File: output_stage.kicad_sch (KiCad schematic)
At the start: 24 parts

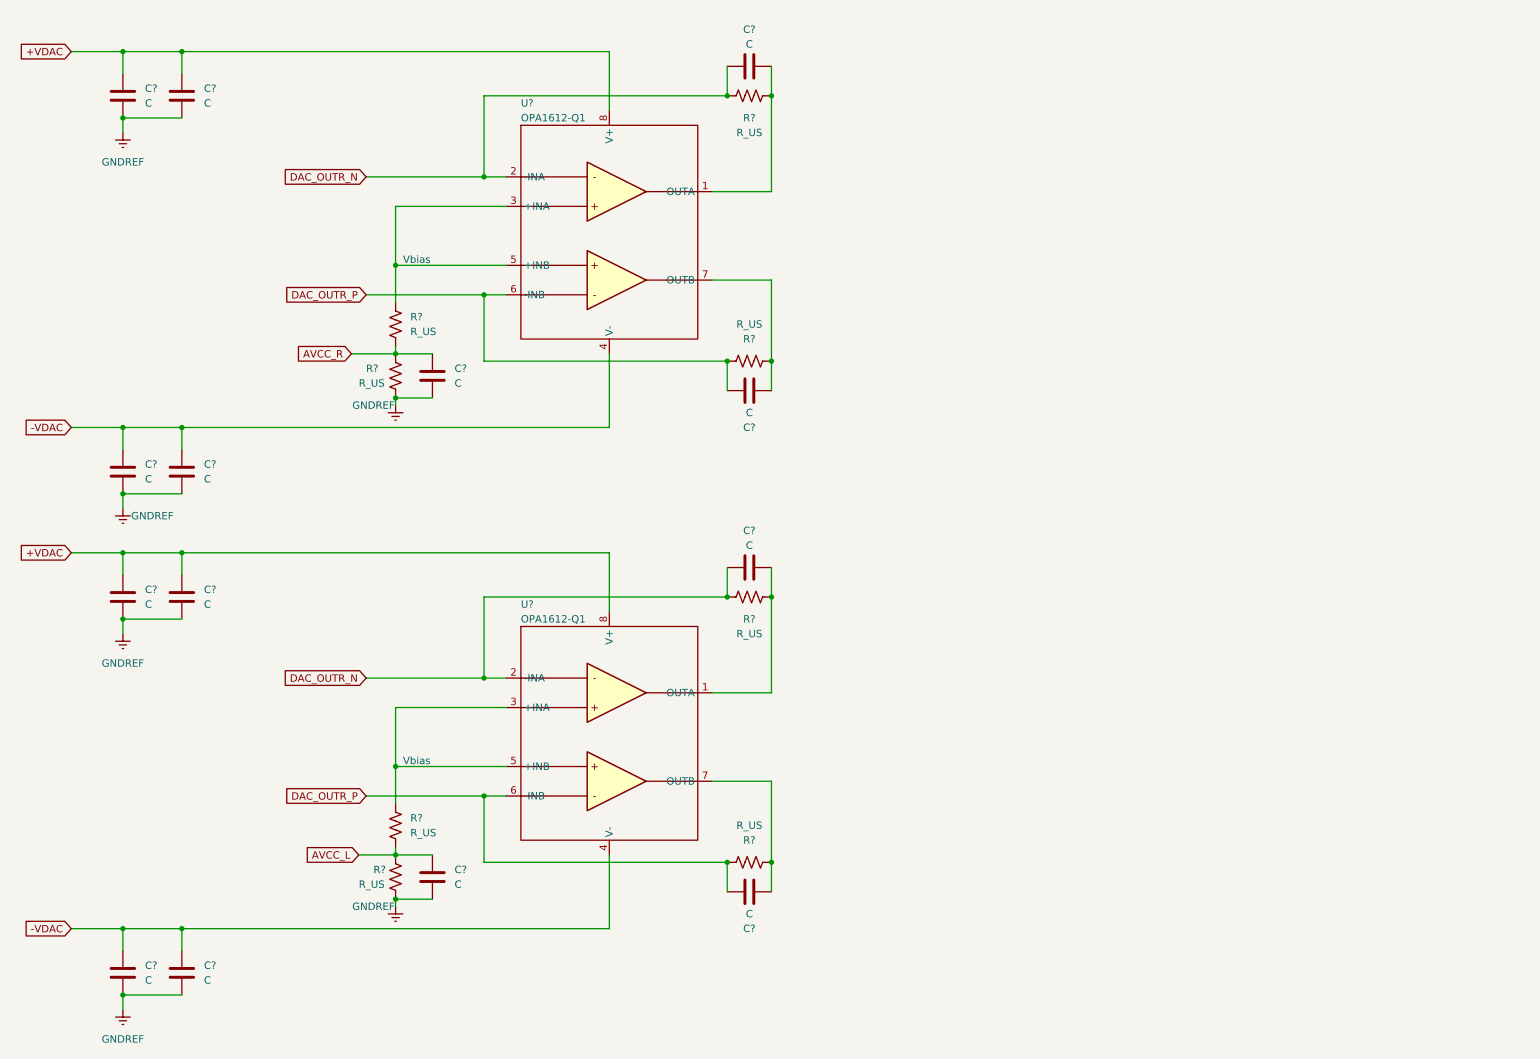
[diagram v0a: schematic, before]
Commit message: Adding values to output stage
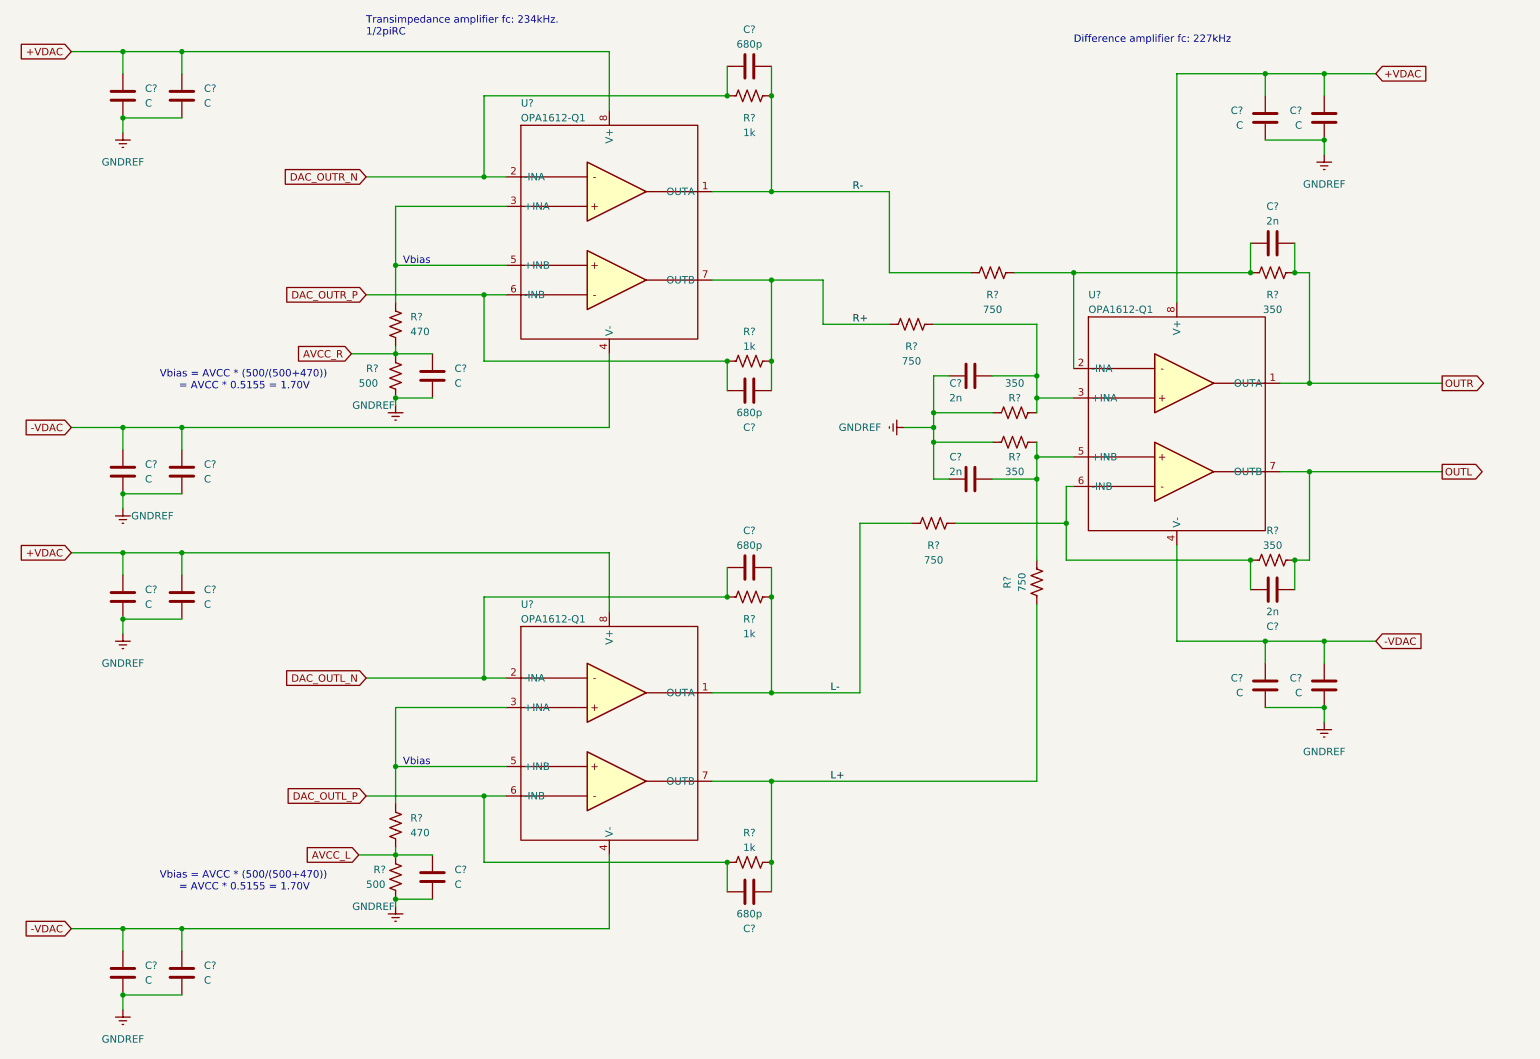
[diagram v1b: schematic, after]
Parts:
- added C? (x4): C, symbol Device:C
- added C? (x4): 2n, symbol Device:C
- added R? (x4): 750, symbol Device:R_US
- added R? (x4): 350, symbol Device:R_US
- added U?: OPA1612-Q1, symbol steDAC:OPA1612-Q1
- C? (x4): value C -> 680p
- R? (x2): value R_US -> 470
- R? (x2): value R_US -> 500
- R? (x4): value R_US -> 1k
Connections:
- net +VDAC: now also C?.2, C?.2, U?.8 (V+)
- net -VDAC: now also C?.2, C?.2, U?.4 (V-)
- net DAC_OUTR_N: no longer C?.2, R?.2, U?.2 (-INA)
- net DAC_OUTR_P: no longer C?.1, R?.1, U?.6 (-INB)
- net GNDREF: now also C?.1, C?.1, C?.1, C?.1, C?.1, C?.2, R?.1, R?.2
- net R+: now reaches C?.2, R?.2, U?.7 (OUTB)
- net R+: now also R?.2
- net R-: now reaches C?.1, R?.1, U?.1 (OUTA)
- net R-: now also R?.2
- net L-: now reaches C?.1, R?.1, U?.1 (OUTA)
- net L-: now also R?.2
- net L+: now reaches C?.2, R?.2, U?.7 (OUTB)
- net L+: now also R?.1
- new net: C?.2, R?.1, R?.2, U?.2 (-INA)
- new net: C?.1, R?.1, R?.1, U?.6 (-INB)
- new net: C?.1, R?.1, R?.2, U?.3 (+INA)
- new net: C?.2, R?.1, R?.2, U?.5 (+INB)
- new net DAC_OUTL_N: C?.2, R?.2, U?.2 (-INA)
- new net DAC_OUTL_P: C?.1, R?.1, U?.6 (-INB)
- new net OUTL: C?.2, R?.2, U?.7 (OUTB)
- new net OUTR: C?.1, R?.1, U?.1 (OUTA)
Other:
- note added: "Difference amplifier fc: 227kHz"
- note added: "Transimpedance amplifier fc: 234kHz. 1/2piRC"
- note added: "Vbias = AVCC * (500/(500+470)) = AVCC * 0.5155 = 1.70V"
- title: SteDAC Output Stage -> Output Stage

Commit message: Redoing power stage and changing output stage accordingly
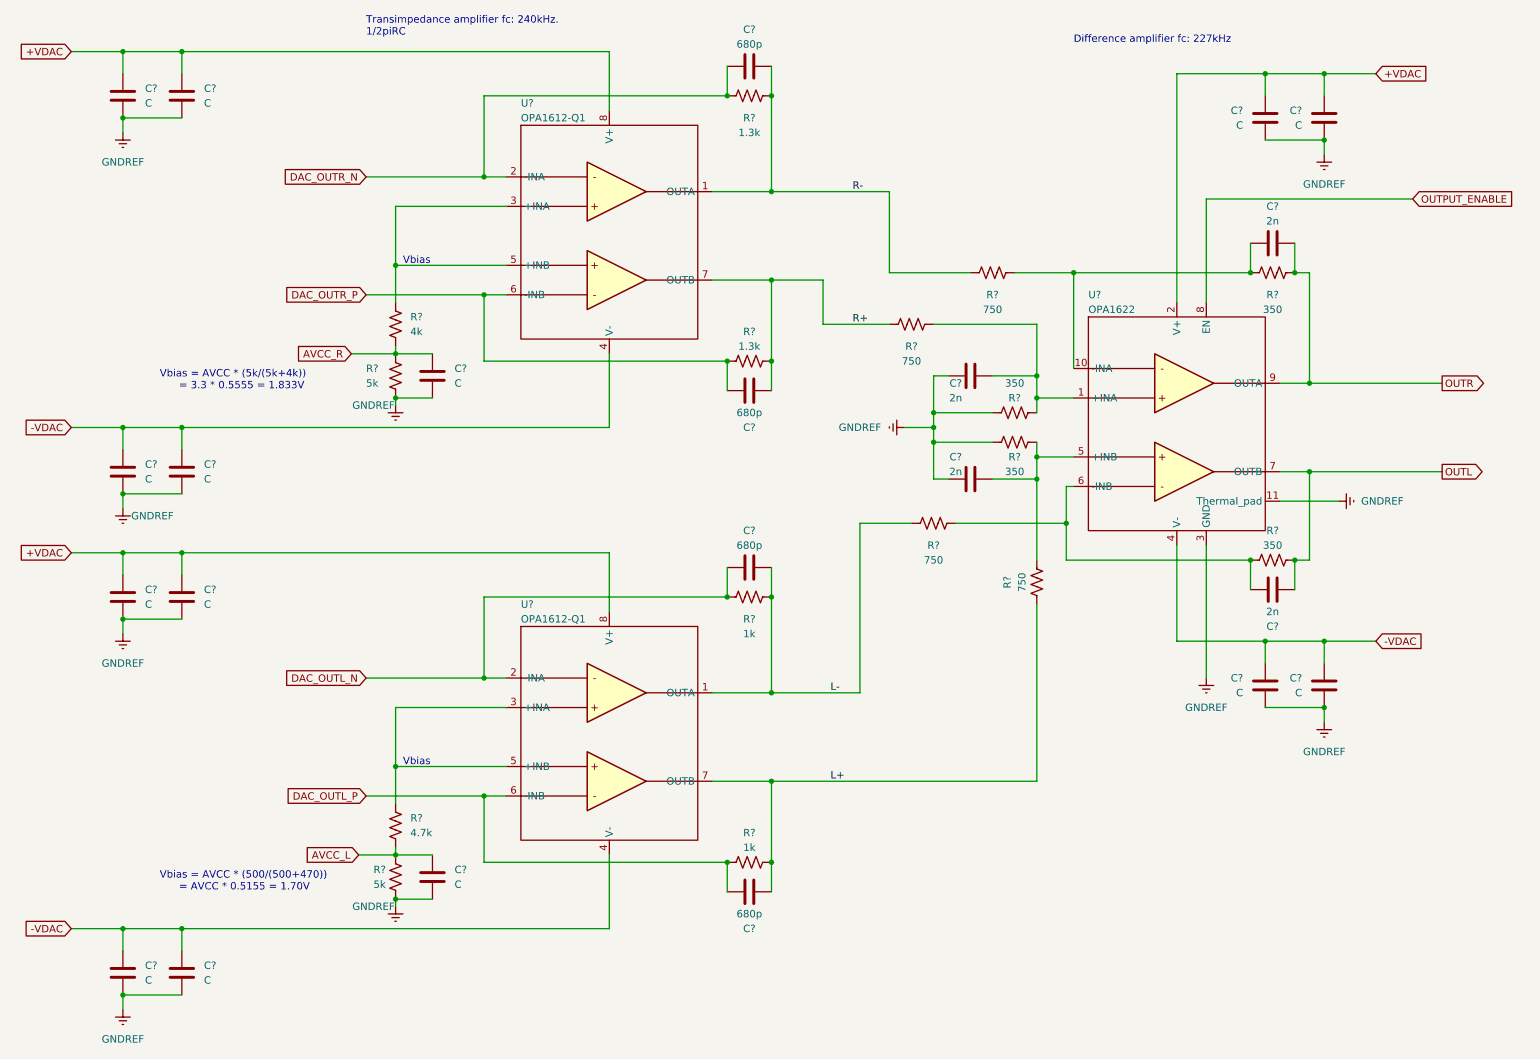
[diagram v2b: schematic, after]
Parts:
- removed U?: OPA1612-Q1, symbol steDAC:OPA1612-Q1
- added U?: OPA1622, symbol steDAC:OPA1622
- R?: value 470 -> 4.7k
- R? (x2): value 500 -> 5k
- R? (x2): value 1k -> 1.3k
- R?: value 470 -> 4k
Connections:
- net +VDAC: now also U?.2 (V+)
- net -VDAC: now also U?.4 (V-)
- net GNDREF: now also U?.11 (Thermal_pad), U?.3 (GND)
- net OUTL: now also U?.7 (OUTB)
- net OUTR: now also U?.9 (OUTA)
- net at C?.2, R?.1, R?.2: now also U?.10 (-INA)
- net at C?.1, R?.1, R?.1: now also U?.6 (-INB)
- net at C?.1, R?.1, R?.2: now also U?.1 (+INA)
- net at C?.2, R?.1, R?.2: now also U?.5 (+INB)
- new net OUTPUT_ENABLE: U?.8 (EN)
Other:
- note added: "Transimpedance amplifier fc: 240kHz. 1/2piRC"
- note added: "Vbias = AVCC * (5k/(5k+4k)) = 3.3 * 0.5555 = 1.833V"
- note removed: "Transimpedance amplifier fc: 234kHz. 1/2piRC"

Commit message: Finishing MCU interface. Adding connectors
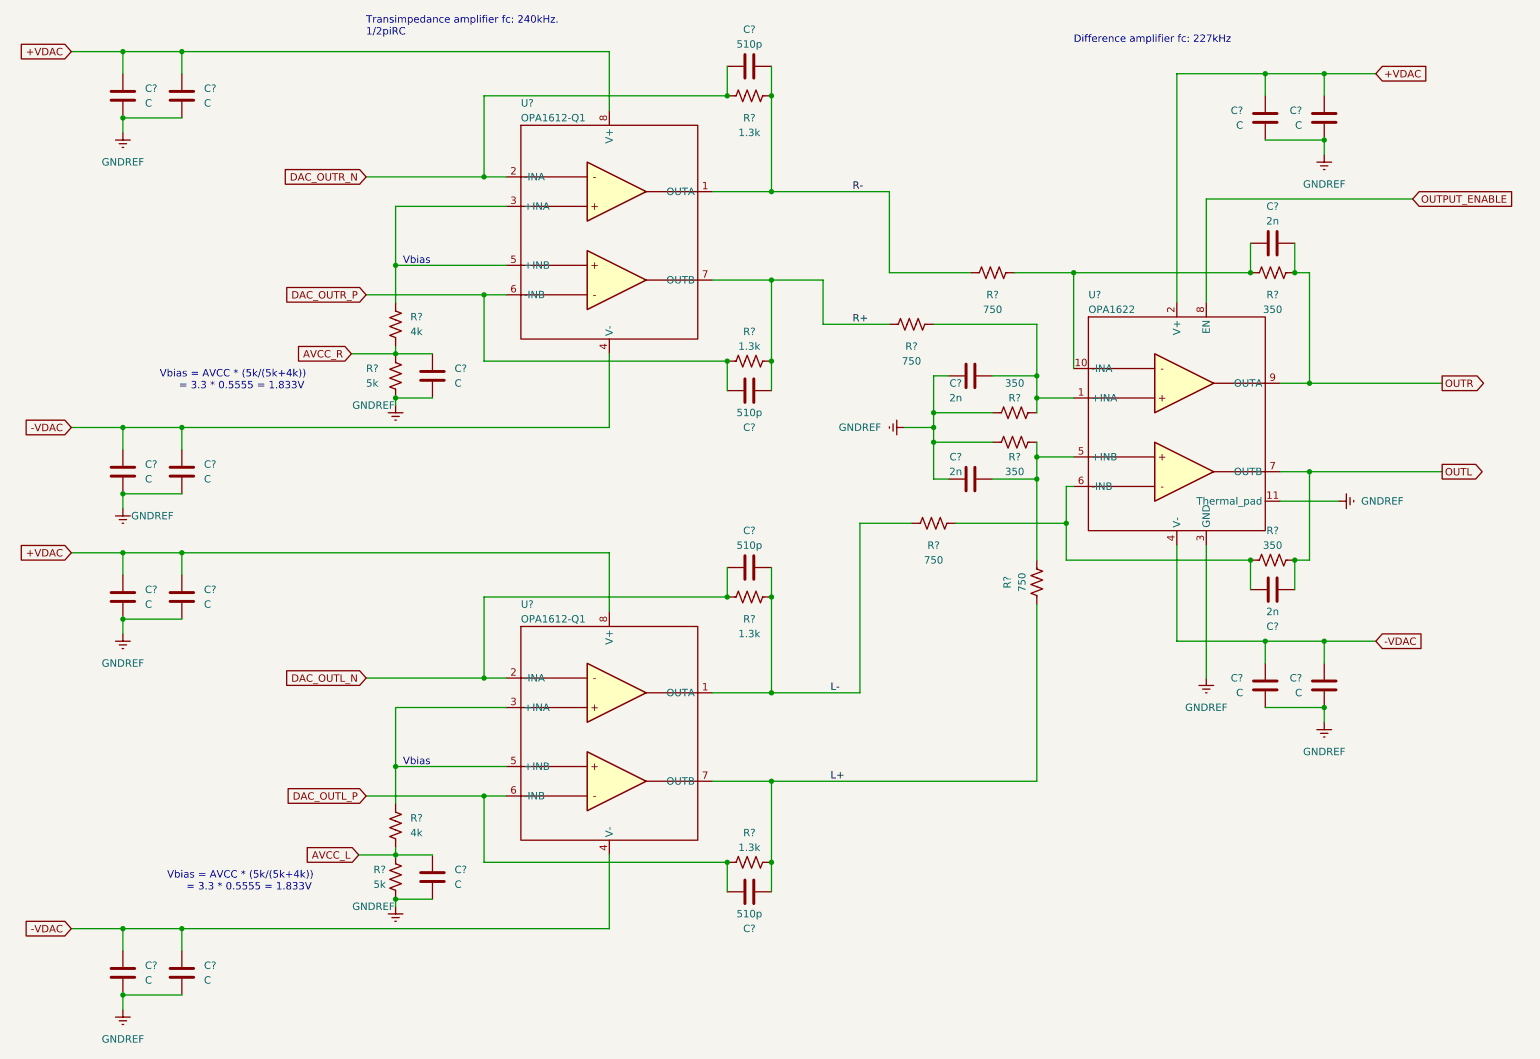
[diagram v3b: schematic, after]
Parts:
- C? (x4): value 680p -> 510p
- R?: value 4.7k -> 4k
- R? (x2): value 1k -> 1.3k
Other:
- note removed: "Vbias = AVCC * (500/(500+470)) = AVCC * 0.5155 = 1.70V"
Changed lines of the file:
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@@
     (stroke (width 0) (type default) (color 0 0 0 0))
   )
-  (text "Vbias = AVCC * (500/(500+470)) \n	  = AVCC * 0.5155 = 1.70V"
-    (at 41.91 163.83 0)
-    (effects (font (size 1.27 1.27)) (justify left bottom))
-  )
   (text "Transimpedance amplifier fc: 240kHz.\n1/2piRC" (at 77.47 16.51 0)
     (effects (font (size 1.27 1.27)) (justify left bottom))
@@
   )
   (text "Vbias" (at 83.82 55.88 0)
+    (effects (font (size 1.27 1.27)) (justify left bottom))
+  )
+  (text "Vbias = AVCC * (5k/(5k+4k)) \n	  = 3.3 * 0.5555 = 1.833V"
+    (at 43.18 163.83 0)
     (effects (font (size 1.27 1.27)) (justify left bottom))
   )
@@
       (effects (font (size 1.27 1.27)) (justify right))
     )
-    (property "Value" "4.7k" (id 1) (at 85.09 153.6699 0)
+    (property "Value" "4k" (id 1) (at 85.09 153.6699 0)
       (effects (font (size 1.27 1.27)) (justify right))
     )
@@
     (in_bom yes) (on_board yes)
     (property "Reference" "C?" (id 0) (at 143.51 83.82 90))
-    (property "Value" "680p" (id 1) (at 143.51 81.28 90))
+    (property "Value" "510p" (id 1) (at 143.51 81.28 90))
     (property "Footprint" "" (id 2) (at 147.32 76.5048 0)
       (effects (font (size 1.27 1.27)) hide)
@@
     (in_bom yes) (on_board yes)
     (property "Reference" "C?" (id 0) (at 143.51 170.18 90))
-    (property "Value" "680p" (id 1) (at 143.51 167.64 90))
+    (property "Value" "510p" (id 1) (at 143.51 167.64 90))
     (property "Footprint" "" (id 2) (at 147.32 162.8648 0)
       (effects (font (size 1.27 1.27)) hide)
@@
     (in_bom yes) (on_board yes)
     (property "Reference" "C?" (id 0) (at 143.51 15.24 90))
-    (property "Value" "680p" (id 1) (at 143.51 17.78 90))
+    (property "Value" "510p" (id 1) (at 143.51 17.78 90))
     (property "Footprint" "" (id 2) (at 139.7 22.5552 0)
       (effects (font (size 1.27 1.27)) hide)
@@
     (in_bom yes) (on_board yes)
     (property "Reference" "C?" (id 0) (at 143.51 101.6 90))
-    (property "Value" "680p" (id 1) (at 143.51 104.14 90))
+    (property "Value" "510p" (id 1) (at 143.51 104.14 90))
     (property "Footprint" "" (id 2) (at 139.7 108.9152 0)
       (effects (font (size 1.27 1.27)) hide)
@@
     (in_bom yes) (on_board yes)
     (property "Reference" "R?" (id 0) (at 143.51 116.84 90))
-    (property "Value" "1k" (id 1) (at 143.51 119.38 90))
+    (property "Value" "1.3k" (id 1) (at 143.51 119.38 90))
     (property "Footprint" "" (id 2) (at 143.256 114.046 90)
       (effects (font (size 1.27 1.27)) hide)
@@
     (in_bom yes) (on_board yes)
     (property "Reference" "R?" (id 0) (at 143.51 153.67 90))
-    (property "Value" "1k" (id 1) (at 143.51 156.21 90))
+    (property "Value" "1.3k" (id 1) (at 143.51 156.21 90))
     (property "Footprint" "" (id 2) (at 143.764 157.734 90)
       (effects (font (size 1.27 1.27)) hide)

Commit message: Finishing Schematic. Fixed ERC errors
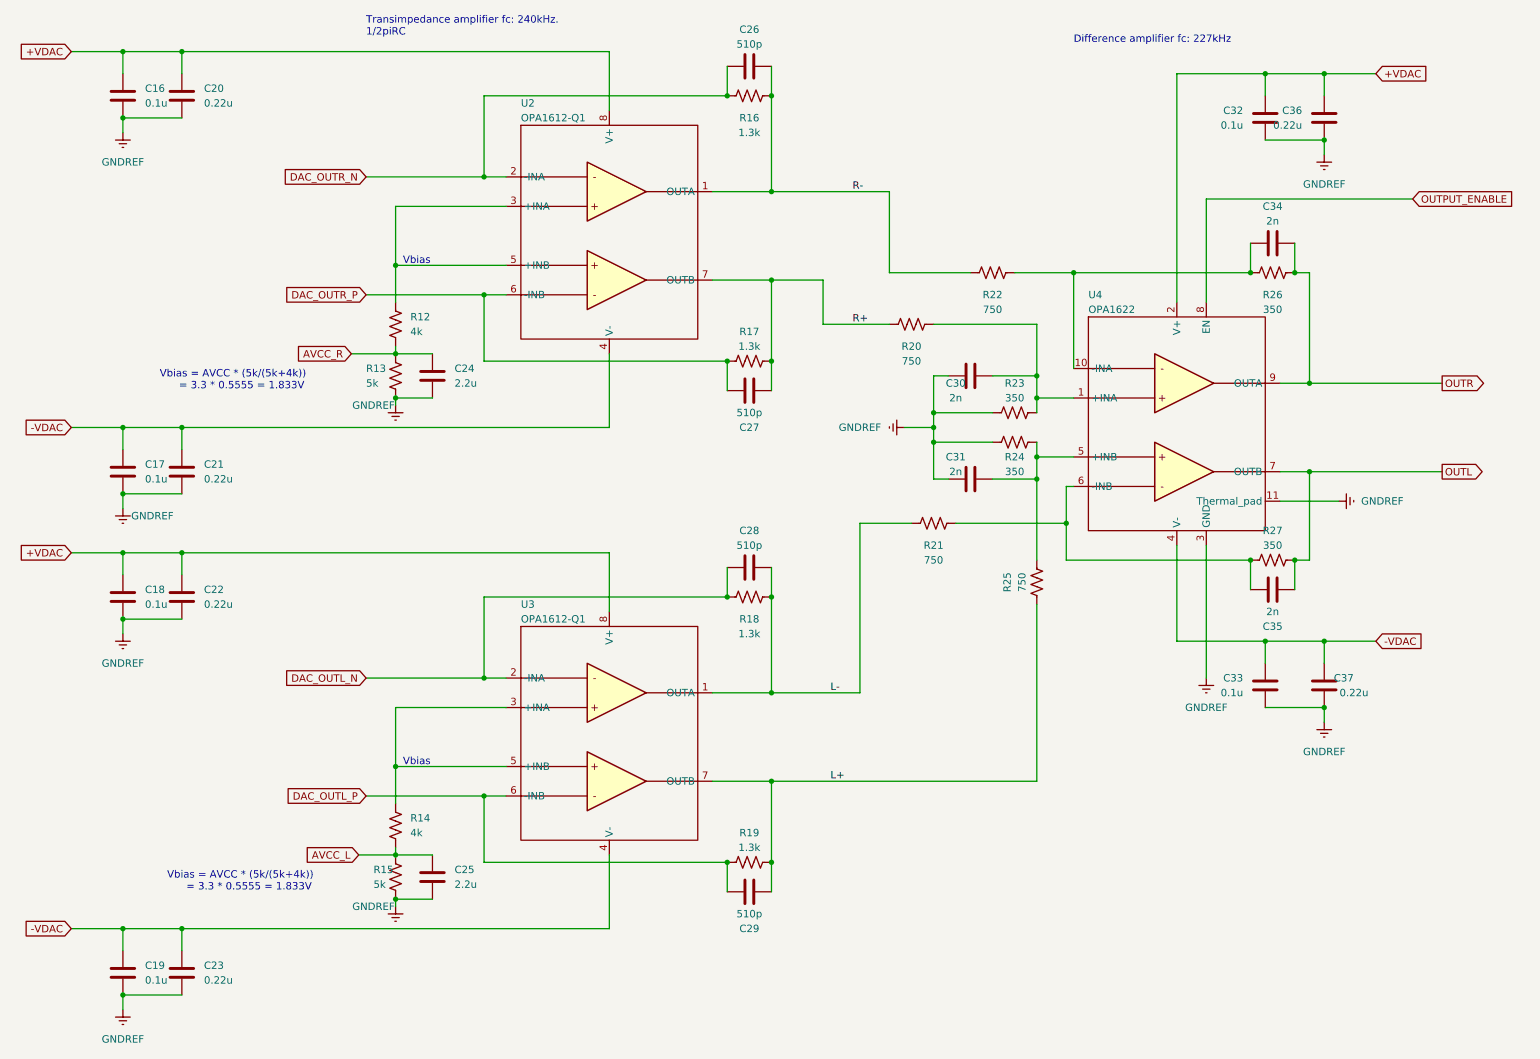
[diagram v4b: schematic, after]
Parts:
- C16, C17, C18, C19, C32, C33: renamed from C?; value C -> 0.1u
- C20, C21, C22, C23, C36, C37: renamed from C?; value C -> 0.22u
- C24, C25: renamed from C?; value C -> 2.2u
- U2, U3: renamed from U?; footprint (none) -> SamacSys_Parts:SOIC127P600X175-8N
- U4: renamed from U?; footprint (none) -> SamacSys_Parts:SON50P300X300X100-11N
- gave numbers to parts that had none: 24

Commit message: Adding footprints
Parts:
- C16, C17, C18, C19, C20, C21, C22, C23, C24, C25, C26, C27, C28, C29, C30, C31, C32, C33, C34, C35, C36, C37: footprint (none) -> Capacitor_SMD:C_0805_2012Metric_Pad1.18x1.45mm_HandSolder
- R12, R13, R14, R15, R16, R17, R18, R19, R20, R21, R22, R23, R24, R25, R26, R27: footprint (none) -> Resistor_SMD:R_0805_2012Metric_Pad1.20x1.40mm_HandSolder
